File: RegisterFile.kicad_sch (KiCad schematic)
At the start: 7 parts, among them U1206 74LS139, U1207 74LS139, U1208 74LS139, U1401 74LS139, U1402 74LS139

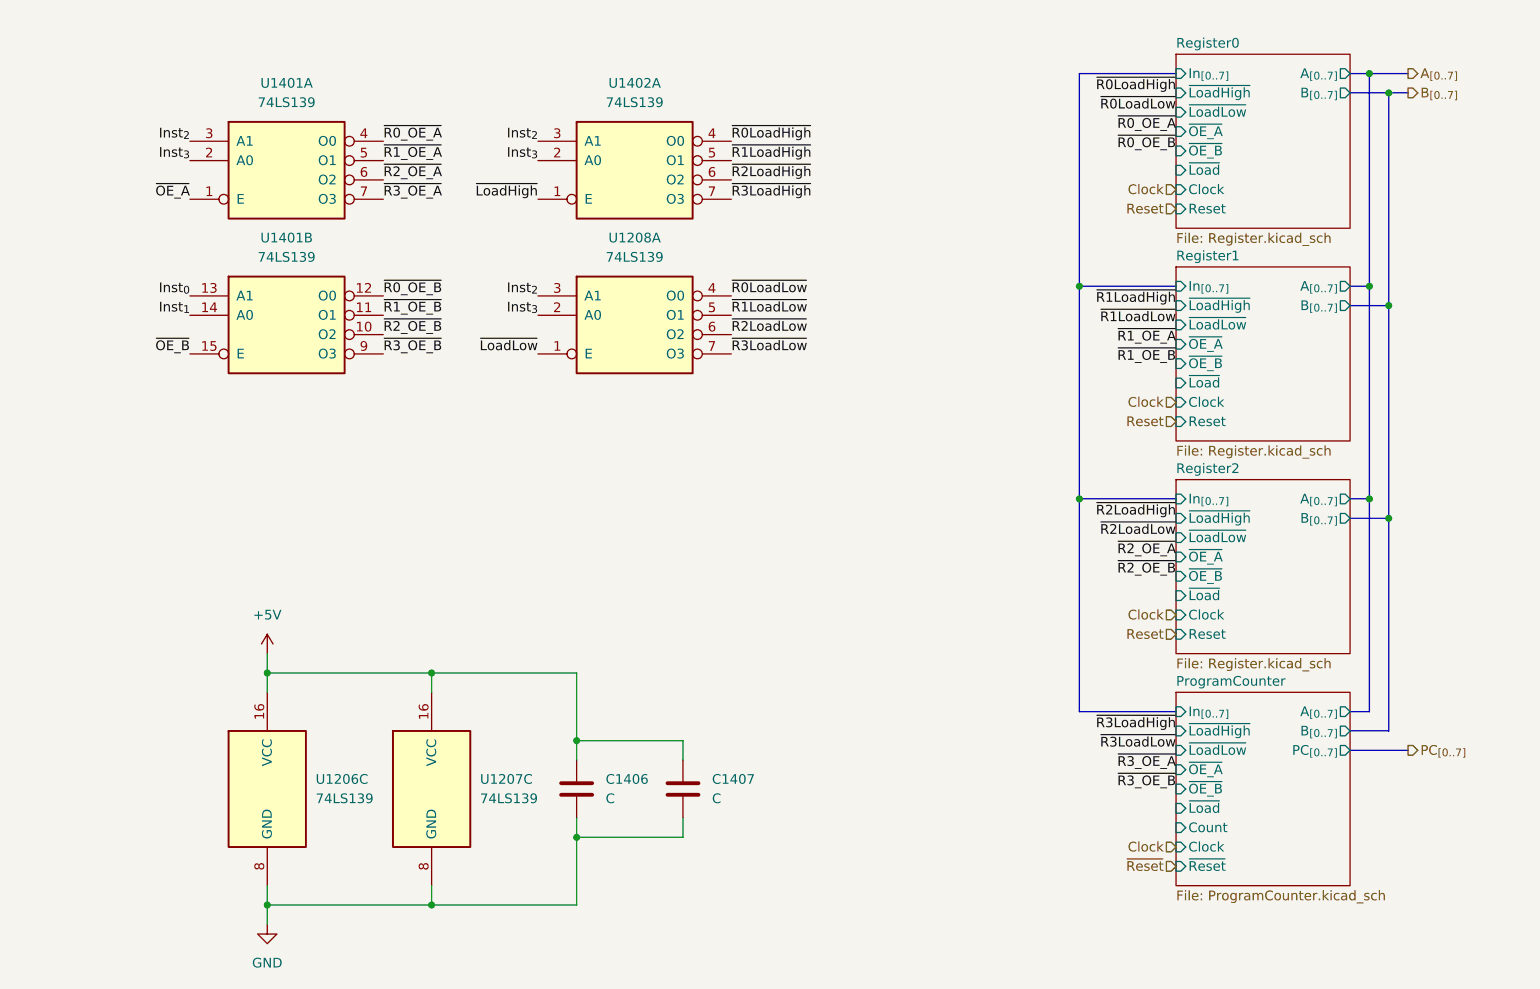
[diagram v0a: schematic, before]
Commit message: Reorganize Registerfile
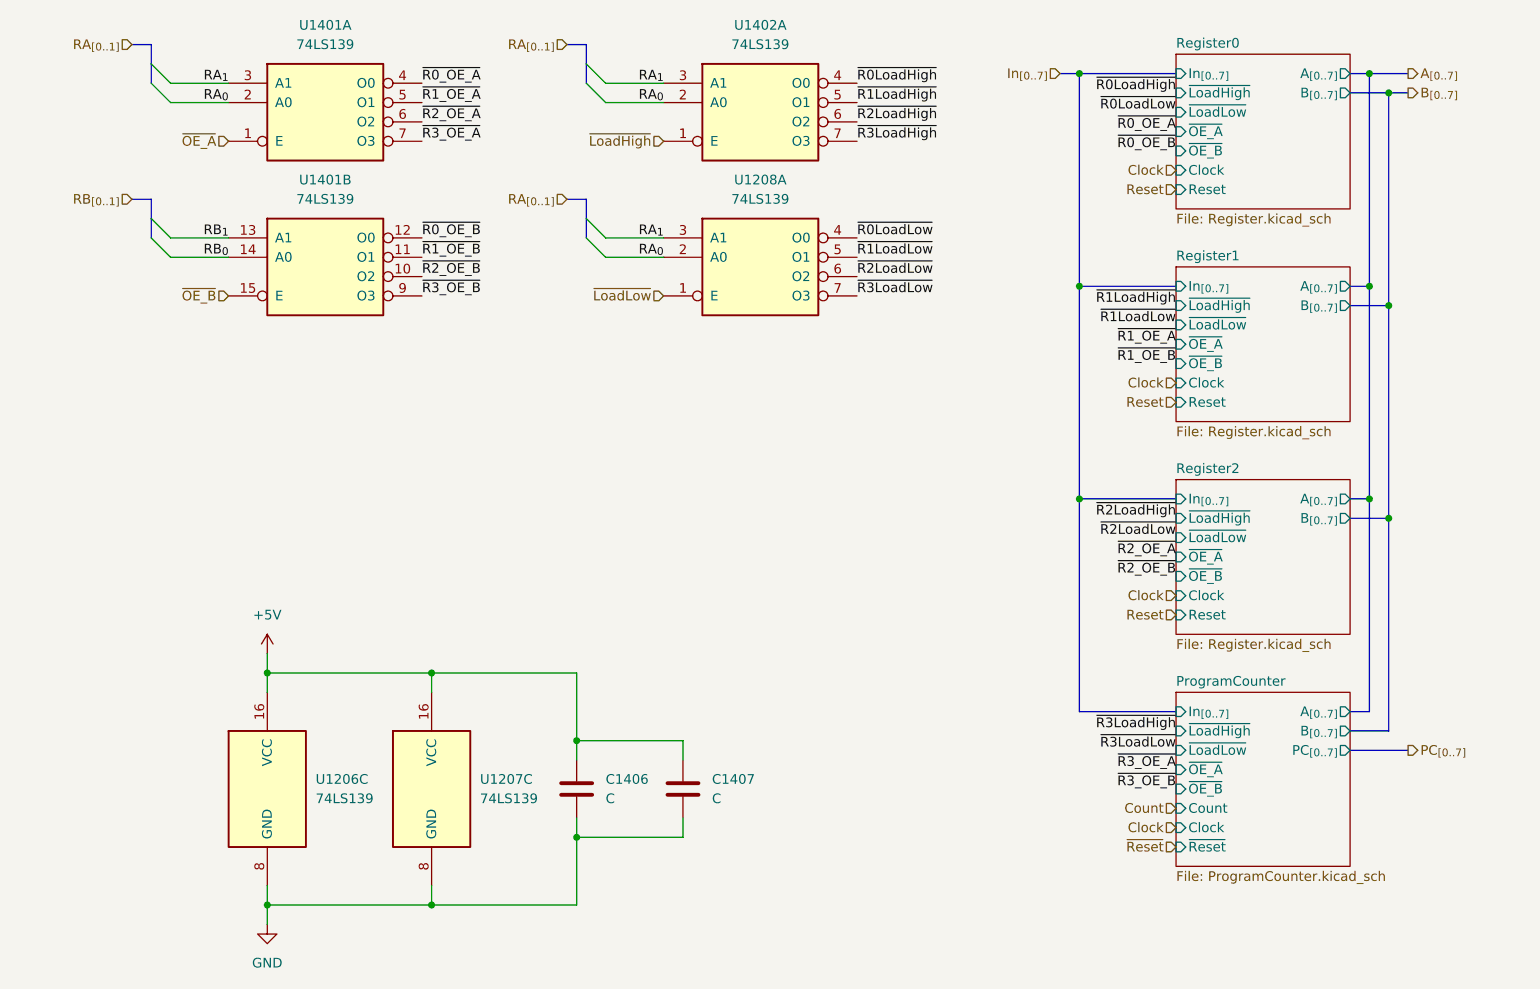
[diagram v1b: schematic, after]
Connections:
- net Inst_{0} renamed RB_{1}
- net Inst_{1} renamed RB_{0}
- net Inst_{2} renamed RA_{1}
- net Inst_{3} renamed RA_{0}
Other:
- sheet ProgramCounter ports: added none; removed ~{Load}
- sheet Register0 ports: added none; removed ~{Load}
- sheet Register1 ports: added none; removed ~{Load}
- sheet Register2 ports: added none; removed ~{Load}
- moved on the sheet: U1208A, U1401A, U1401B, U1402A

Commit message: More cleanup and preparing signals for control logic
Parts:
- renumbered C1406 to C1401, C1407 to C1402, U1206 to U1401, U1207 to U1402, U1208 to U1403
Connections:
- net ~{OE_A} is gone; now on net GND: U1401.1 (E)
- net ~{OE_B} is gone; now on net GND: U1401.15 (E)
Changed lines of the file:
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@@
+		)
+	)
+	(wire
+		(pts
+			(xy 34.29 30.48) (xy 33.02 30.48)
+		)
+		(stroke
+			(width 0)
+			(type default)
+		)
+	)
+	(wire
+		(pts
+			(xy 33.02 30.48) (xy 33.02 31.75)
+		)
+		(stroke
+			(width 0)
+			(type default)
 		)
 	)
@@
 		)
 	)
+	(wire
+		(pts
+			(xy 33.02 50.8) (xy 33.02 52.07)
+		)
+		(stroke
+			(width 0)
+			(type default)
+		)
+	)
 	(bus
 		(pts
@@
 		(pts
 			(xy 24.13 22.86) (xy 24.13 20.32)
+		)
+		(stroke
+			(width 0)
+			(type default)
+		)
+	)
+	(wire
+		(pts
+			(xy 34.29 50.8) (xy 33.02 50.8)
 		)
 		(stroke
@@
 		)
 	)
-	(hierarchical_label "~{OE_A}"
-		(shape input)
-		(at 34.29 30.48 180)
-		(effects
-			(font
-				(size 1.27 1.27)
-			)
-			(justify right)
-		)
-	)
 	(hierarchical_label "Clock"
 		(shape input)
@@
 		(shape input)
 		(at 158.75 64.77 180)
-		(effects
-			(font
-				(size 1.27 1.27)
-			)
-			(justify right)
-		)
-	)
-	(hierarchical_label "~{OE_B}"
-		(shape input)
-		(at 34.29 50.8 180)
 		(effects
 			(font
@@
 	)
 	(symbol
+		(lib_id "power:GND")
+		(at 33.02 31.75 0)
+		(unit 1)
+		(exclude_from_sim no)
+		(in_bom yes)
+		(on_board yes)
+		(dnp no)
+		(fields_autoplaced yes)
+		(property "Reference" "#PWR01401"
+			(at 33.02 38.1 0)
+			(effects
+				(font
+					(size 1.27 1.27)
+				)
+				(hide yes)
+			)
+		)
+		(property "Value" "GND"
+			(at 33.02 36.83 0)
+			(effects
+				(font
+					(size 1.27 1.27)
+				)
+			)
+		)
+		(property "Footprint" ""
+			(at 33.02 31.75 0)
+			(effects
+				(font
+					(size 1.27 1.27)
+				)
+				(hide yes)
+			)
+		)
+		(property "Datasheet" ""
+			(at 33.02 31.75 0)
+			(effects
+				(font
+					(size 1.27 1.27)
+				)
+				(hide yes)
+			)
+		)
+		(property "Description" "Power symbol creates a global label with name \"GND\" , ground"
+			(at 33.02 31.75 0)
+			(effects
+				(font
+					(size 1.27 1.27)
+				)
+				(hide yes)
+			)
+		)
+		(pin "1"
+		)
+		(instances
+			(project "BRISC8"
+				(path "/e198223b-f7bd-4b26-ae2e-259db8d07fb6/d081cdcb-1181-4657-9580-dc3ba9a85775/ded358fb-ee52-4096-a32a-0cce52708100"
+					(reference "#PWR01401")
+					(unit 1)
+				)
+			)
+		)
+	)
+	(symbol
 		(lib_id "74xx:74LS139")
 		(at 60.96 115.57 0)
@@
 		(dnp no)
 		(fields_autoplaced yes)
-		(property "Reference" "U1207"
+		(property "Reference" "U1402"
 			(at 67.31 114.2999 0)
 			(effects
@@
 			(project "BRISC8"
 				(path "/e198223b-f7bd-4b26-ae2e-259db8d07fb6/d081cdcb-1181-4657-9580-dc3ba9a85775/ded358fb-ee52-4096-a32a-0cce52708100"
-					(reference "U1207")
+					(reference "U1402")
 					(unit 3)
 				)
@@
 		(dnp no)
 		(fields_autoplaced yes)
-		(property "Reference" "#PWR01420"
+		(property "Reference" "#PWR01403"
 			(at 39.37 101.6 0)
 			(effects
@@
 			(project ""
 				(path "/e198223b-f7bd-4b26-ae2e-259db8d07fb6/d081cdcb-1181-4657-9580-dc3ba9a85775/ded358fb-ee52-4096-a32a-0cce52708100"
-					(reference "#PWR01420")
+					(reference "#PWR01403")
 					(unit 1)
 				)
@@
 		(dnp no)
 		(fields_autoplaced yes)
-		(property "Reference" "U1208"
+		(property "Reference" "U1403"
 			(at 104.14 35.56 0)
 			(effects
@@
 			(project "BRISC8"
 				(path "/e198223b-f7bd-4b26-ae2e-259db8d07fb6/d081cdcb-1181-4657-9580-dc3ba9a85775/ded358fb-ee52-4096-a32a-0cce52708100"
-					(reference "U1208")
+					(reference "U1403")
 					(unit 1)
 				)
@@
 		(dnp no)
 		(fields_autoplaced yes)
-		(property "Reference" "#PWR01419"
+		(property "Reference" "#PWR01404"
 			(at 39.37 139.7 0)
 			(effects
@@
 			(project ""
 				(path "/e198223b-f7bd-4b26-ae2e-259db8d07fb6/d081cdcb-1181-4657-9580-dc3ba9a85775/ded358fb-ee52-4096-a32a-0cce52708100"
-					(reference "#PWR01419")
+					(reference "#PWR01404")
 					(unit 1)
 				)
@@
 		(dnp no)
 		(fields_autoplaced yes)
-		(property "Reference" "U1206"
+		(property "Reference" "U1401"
 			(at 45.72 114.2999 0)
 			(effects
@@
 			(project "BRISC8"
 				(path "/e198223b-f7bd-4b26-ae2e-259db8d07fb6/d081cdcb-1181-4657-9580-dc3ba9a85775/ded358fb-ee52-4096-a32a-0cce52708100"
-					(reference "U1206")
+					(reference "U1401")
 					(unit 3)
+				)
+			)
+		)
+	)
+	(symbol
+		(lib_id "power:GND")
+		(at 33.02 52.07 0)
+		(unit 1)
+		(exclude_from_sim no)
+		(in_bom yes)
+		(on_board yes)
+		(dnp no)
+		(fields_autoplaced yes)
+		(property "Reference" "#PWR01402"
+			(at 33.02 58.42 0)
+			(effects
+				(font
+					(size 1.27 1.27)
+				)
+				(hide yes)
+			)
+		)
+		(property "Value" "GND"
+			(at 33.02 57.15 0)
+			(effects
+				(font
+					(size 1.27 1.27)
+				)
+			)
+		)
+		(property "Footprint" ""
+			(at 33.02 52.07 0)
+			(effects
+				(font
+					(size 1.27 1.27)
+				)
+				(hide yes)
+			)
+		)
+		(property "Datasheet" ""
+			(at 33.02 52.07 0)
+			(effects
+				(font
+					(size 1.27 1.27)
+				)
+				(hide yes)
+			)
+		)
+		(property "Description" "Power symbol creates a global label with name \"GND\" , ground"
+			(at 33.02 52.07 0)
+			(effects
+				(font
+					(size 1.27 1.27)
+				)
+				(hide yes)
+			)
+		)
+		(pin "1"
+		)
+		(instances
+			(project ""
+				(path "/e198223b-f7bd-4b26-ae2e-259db8d07fb6/d081cdcb-1181-4657-9580-dc3ba9a85775/ded358fb-ee52-4096-a32a-0cce52708100"
+					(reference "#PWR01402")
+					(unit 1)
 				)
 			)
@@
 		(dnp no)
 		(fields_autoplaced yes)
-		(property "Reference" "C1406"
+		(property "Reference" "C1401"
 			(at 83.82 114.2999 0)
 			(effects
@@
 			(project ""
 				(path "/e198223b-f7bd-4b26-ae2e-259db8d07fb6/d081cdcb-1181-4657-9580-dc3ba9a85775/ded358fb-ee52-4096-a32a-0cce52708100"
-					(reference "C1406")
+					(reference "C1401")
 					(unit 1)
 				)
@@
 		(dnp no)
 		(fields_autoplaced yes)
-		(property "Reference" "C1407"
+		(property "Reference" "C1402"
 			(at 97.79 114.2999 0)
 			(effects
@@
 			(project "BRISC8"
 				(path "/e198223b-f7bd-4b26-ae2e-259db8d07fb6/d081cdcb-1181-4657-9580-dc3ba9a85775/ded358fb-ee52-4096-a32a-0cce52708100"
-					(reference "C1407")
+					(reference "C1402")
 					(unit 1)
 				)

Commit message: Draft Schematic
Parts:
- C1401, C1402: value C -> 0.1uF; footprint (none) -> Capacitor_THT:C_Rect_L4.0mm_W2.5mm_P2.50mm
- U1401, U1402: value 74LS139 -> 74HC139; footprint (none) -> Package_DIP:DIP-16_W7.62mm
- U1402: renamed from U1403; value 74LS139 -> 74HC139; footprint (none) -> Package_DIP:DIP-16_W7.62mm
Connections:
- net RA_{0}: now also U1402.14 (A0); no longer U1402.2 (A0)
- net RA_{1}: now also U1402.13 (A1); no longer U1402.3 (A1)
- net ~{LoadLow}: now also U1402.15 (E); no longer U1402.1 (E)
- net ~{R0LoadLow}: now also U1402.12 (O0); no longer U1402.4 (O0)
- net ~{R1LoadLow}: now also U1402.11 (O1); no longer U1402.5 (O1)
- net ~{R2LoadLow}: now also U1402.10 (O2); no longer U1402.6 (O2)
- net ~{R3LoadLow}: now also U1402.9 (O3); no longer U1402.7 (O3)
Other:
- company: (none) -> Brian Duffy
- title: (none) -> BRISC8 CPU
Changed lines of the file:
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@@
 	(generator "eeschema")
 	(generator_version "9.0")
-	(paper "A4")
+	(paper "USLetter")
+	(title_block
+		(title "BRISC8 CPU")
+		(date "2025-06-26")
+		(rev "v1.0.0")
+		(company "Brian Duffy")
+		(comment 3 "Compatible with the BRISC8 assembler and compiler suite.")
+		(comment 4 "Simple 8-bit RISC CPU designed by Brian Duffy to explore the lowest level of computing.")
+	)
 	(junction
 		(at 39.37 100.33)
@@
 			)
 		)
-		(property "Value" "74LS139"
+		(property "Value" "74HC139"
 			(at 104.14 17.78 0)
 			(effects
@@
 			)
 		)
-		(property "Footprint" ""
+		(property "Footprint" "Package_DIP:DIP-16_W7.62mm"
 			(at 104.14 25.4 0)
 			(effects
@@
 			)
 		)
-		(property "Value" "74LS139"
+		(property "Value" "74HC139"
 			(at 46.99 38.1 0)
 			(effects
@@
 			)
 		)
-		(property "Footprint" ""
+		(property "Footprint" "Package_DIP:DIP-16_W7.62mm"
 			(at 46.99 45.72 0)
 			(effects
@@
 			)
 		)
-		(property "Value" "74LS139"
+		(property "Value" "74HC139"
 			(at 67.31 116.8399 0)
 			(effects
@@
 			)
 		)
-		(property "Footprint" ""
+		(property "Footprint" "Package_DIP:DIP-16_W7.62mm"
 			(at 60.96 115.57 0)
 			(effects
@@
 		(lib_id "74xx:74LS139")
 		(at 104.14 45.72 0)
-		(unit 1)
+		(unit 2)
 		(exclude_from_sim no)
 		(in_bom yes)
@@
 		(dnp no)
 		(fields_autoplaced yes)
-		(property "Reference" "U1403"
+		(property "Reference" "U1402"
 			(at 104.14 35.56 0)
 			(effects
@@
 			)
 		)
-		(property "Value" "74LS139"
+		(property "Value" "74HC139"
 			(at 104.14 38.1 0)
 			(effects
@@
 			)
 		)
-		(property "Footprint" ""
+		(property "Footprint" "Package_DIP:DIP-16_W7.62mm"
 			(at 104.14 45.72 0)
 			(effects
@@
 			(project "BRISC8"
 				(path "/e198223b-f7bd-4b26-ae2e-259db8d07fb6/d081cdcb-1181-4657-9580-dc3ba9a85775/ded358fb-ee52-4096-a32a-0cce52708100"
-					(reference "U1403")
-					(unit 1)
+					(reference "U1402")
+					(unit 2)
 				)
 			)
@@
 			)
 		)
-		(property "Value" "74LS139"
+		(property "Value" "74HC139"
 			(at 45.72 116.8399 0)
 			(effects
@@
 			)
 		)
-		(property "Footprint" ""
+		(property "Footprint" "Package_DIP:DIP-16_W7.62mm"
 			(at 39.37 115.57 0)
 			(effects
@@
 			)
 		)
-		(property "Value" "C"
+		(property "Value" "0.1uF"
 			(at 83.82 116.8399 0)
 			(effects
@@
 			)
 		)
-		(property "Footprint" ""
+		(property "Footprint" "Capacitor_THT:C_Rect_L4.0mm_W2.5mm_P2.50mm"
 			(at 80.9752 119.38 0)
 			(effects
@@
 			)
 		)
-		(property "Value" "74LS139"
+		(property "Value" "74HC139"
 			(at 46.99 17.78 0)
 			(effects
@@
 			)
 		)
-		(property "Footprint" ""
+		(property "Footprint" "Package_DIP:DIP-16_W7.62mm"
 			(at 46.99 25.4 0)
 			(effects
@@
 			)
 		)
-		(property "Value" "C"
+		(property "Value" "0.1uF"
 			(at 97.79 116.8399 0)
 			(effects
@@
 			)
 		)
-		(property "Footprint" ""
+		(property "Footprint" "Capacitor_THT:C_Rect_L4.0mm_W2.5mm_P2.50mm"
 			(at 94.9452 119.38 0)
 			(effects
